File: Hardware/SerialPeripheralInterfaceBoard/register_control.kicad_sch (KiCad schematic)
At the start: 3 parts, among them U4 74HC04, U6 74HC574, U7 74HC574

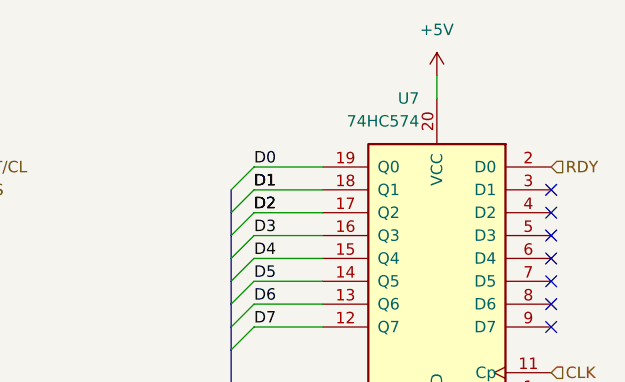
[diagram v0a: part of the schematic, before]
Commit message: feat: modify mother board for paging and dma
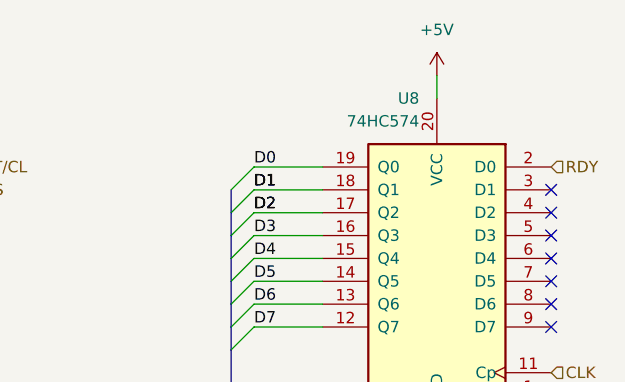
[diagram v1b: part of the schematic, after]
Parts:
- renumbered U7 to U8
